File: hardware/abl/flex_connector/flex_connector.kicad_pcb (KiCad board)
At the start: 2 copper layers, 68.3 x 119.1 mm, 3 parts, among them J1 Conn_01x20_Pin, J2 Conn_01x20_Pin

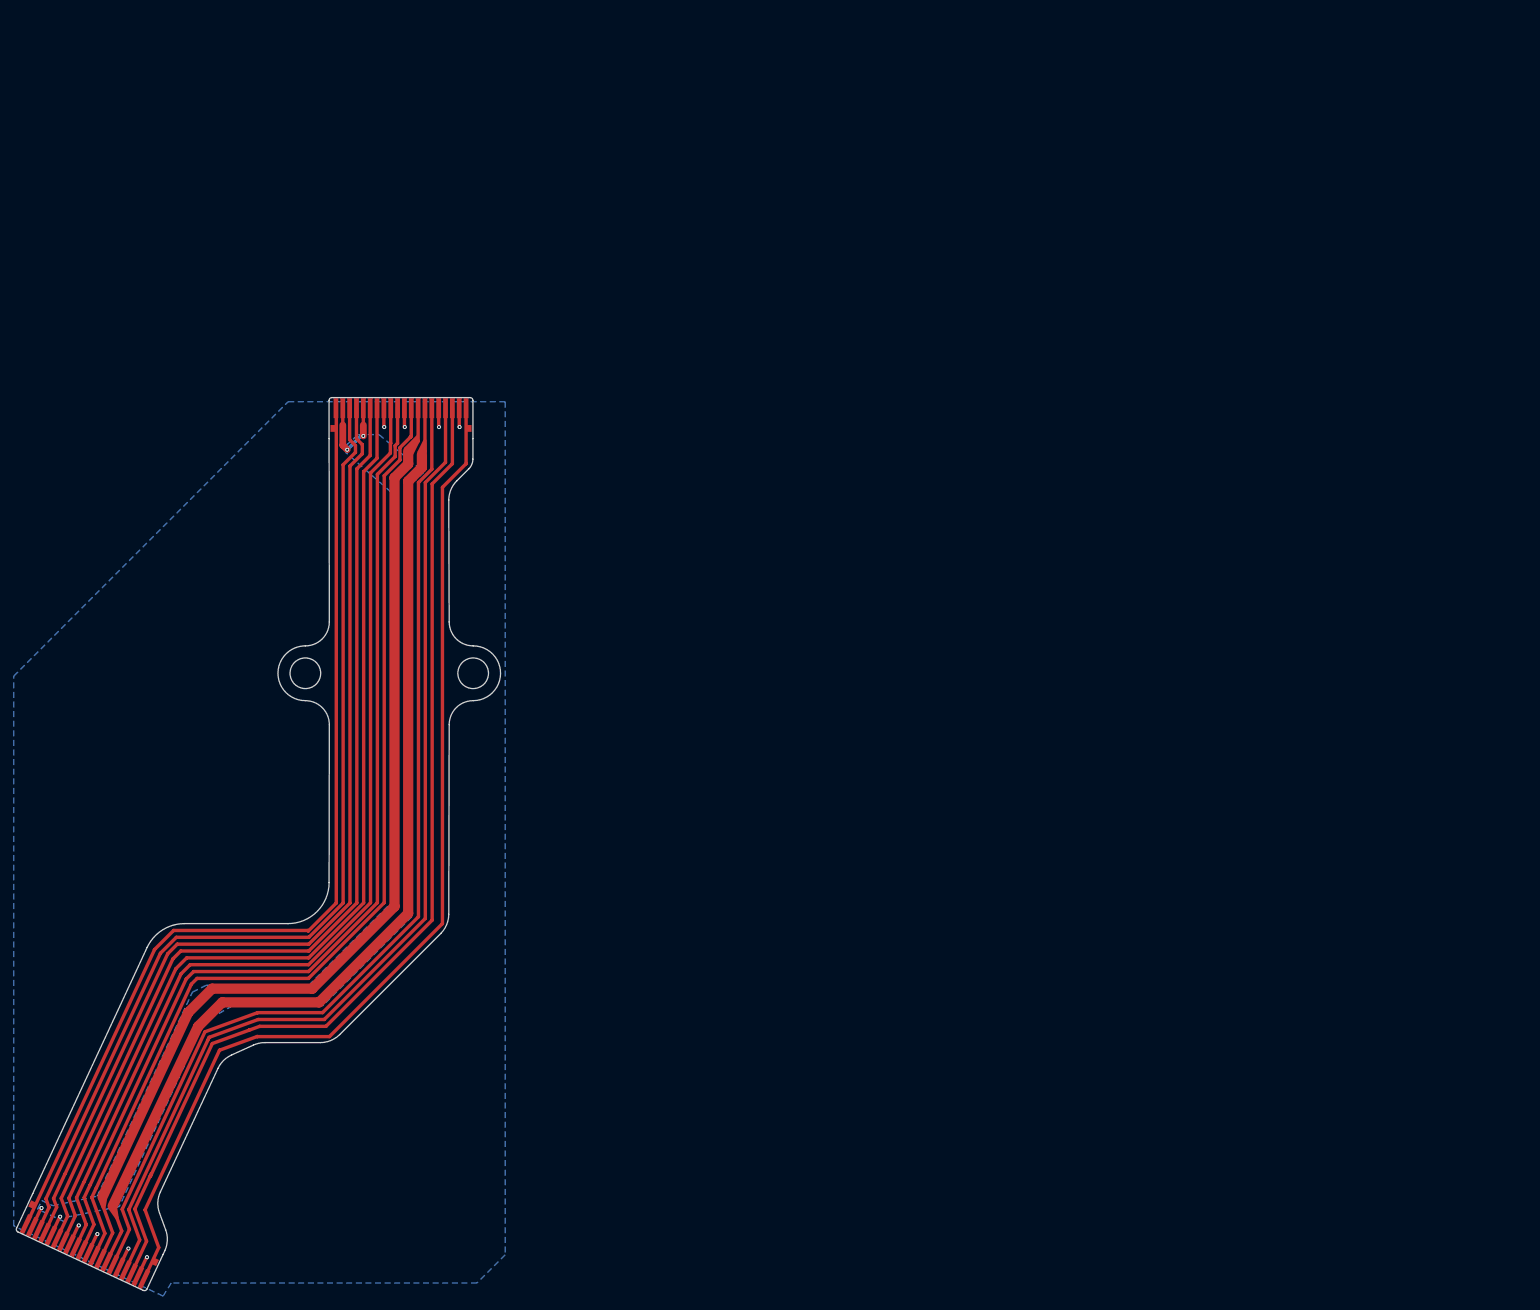
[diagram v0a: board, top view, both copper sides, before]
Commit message: Rename files, names and labels to be more consistent. Add READMEs for connectors and extend some other READMEs.
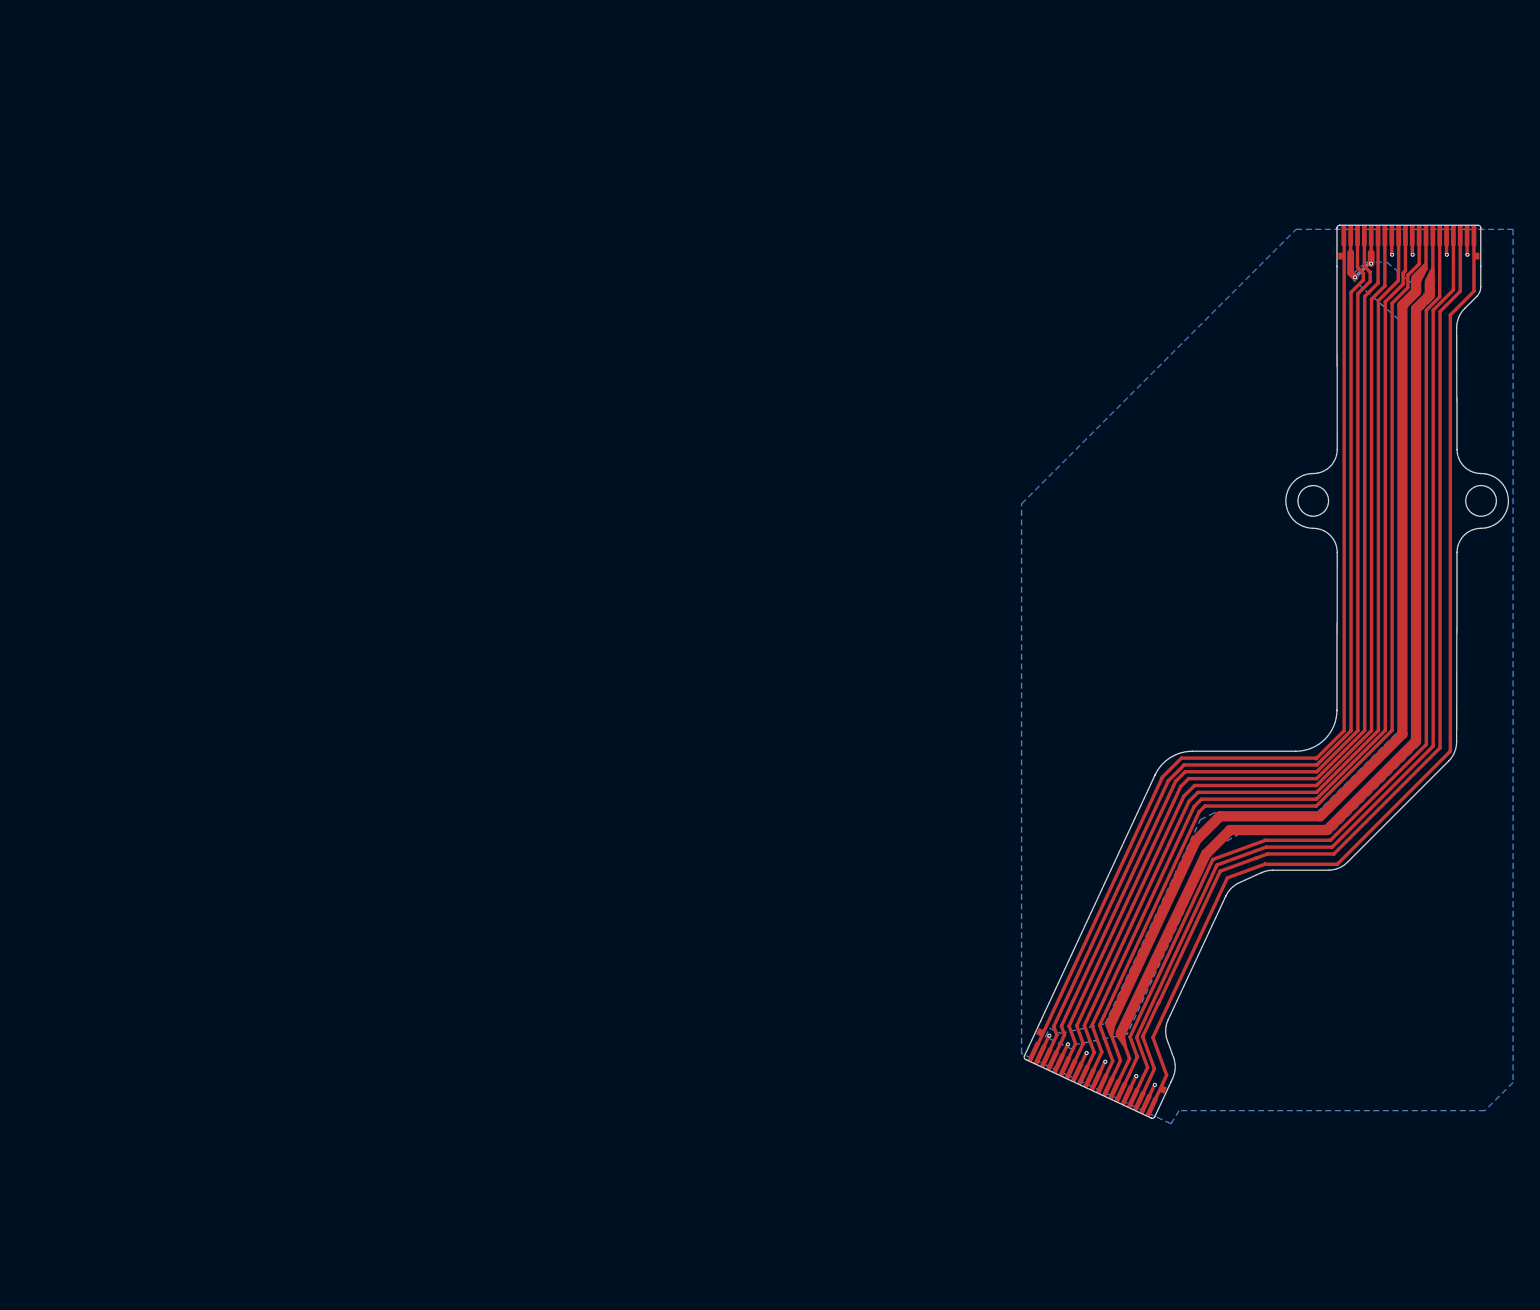
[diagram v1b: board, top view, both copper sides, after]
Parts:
- moved G*** 149.3 mm to (214.5, 93.2)
- moved J1 149.3 mm to (181.7, 163.0)
- moved J2 149.3 mm to (209.1, 38.6)
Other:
- board text added: "ABL Flex Connector v1.0"
- board text removed: "Flex Connector A v1.0"

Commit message: Add current renderings to all ABL PCBs.
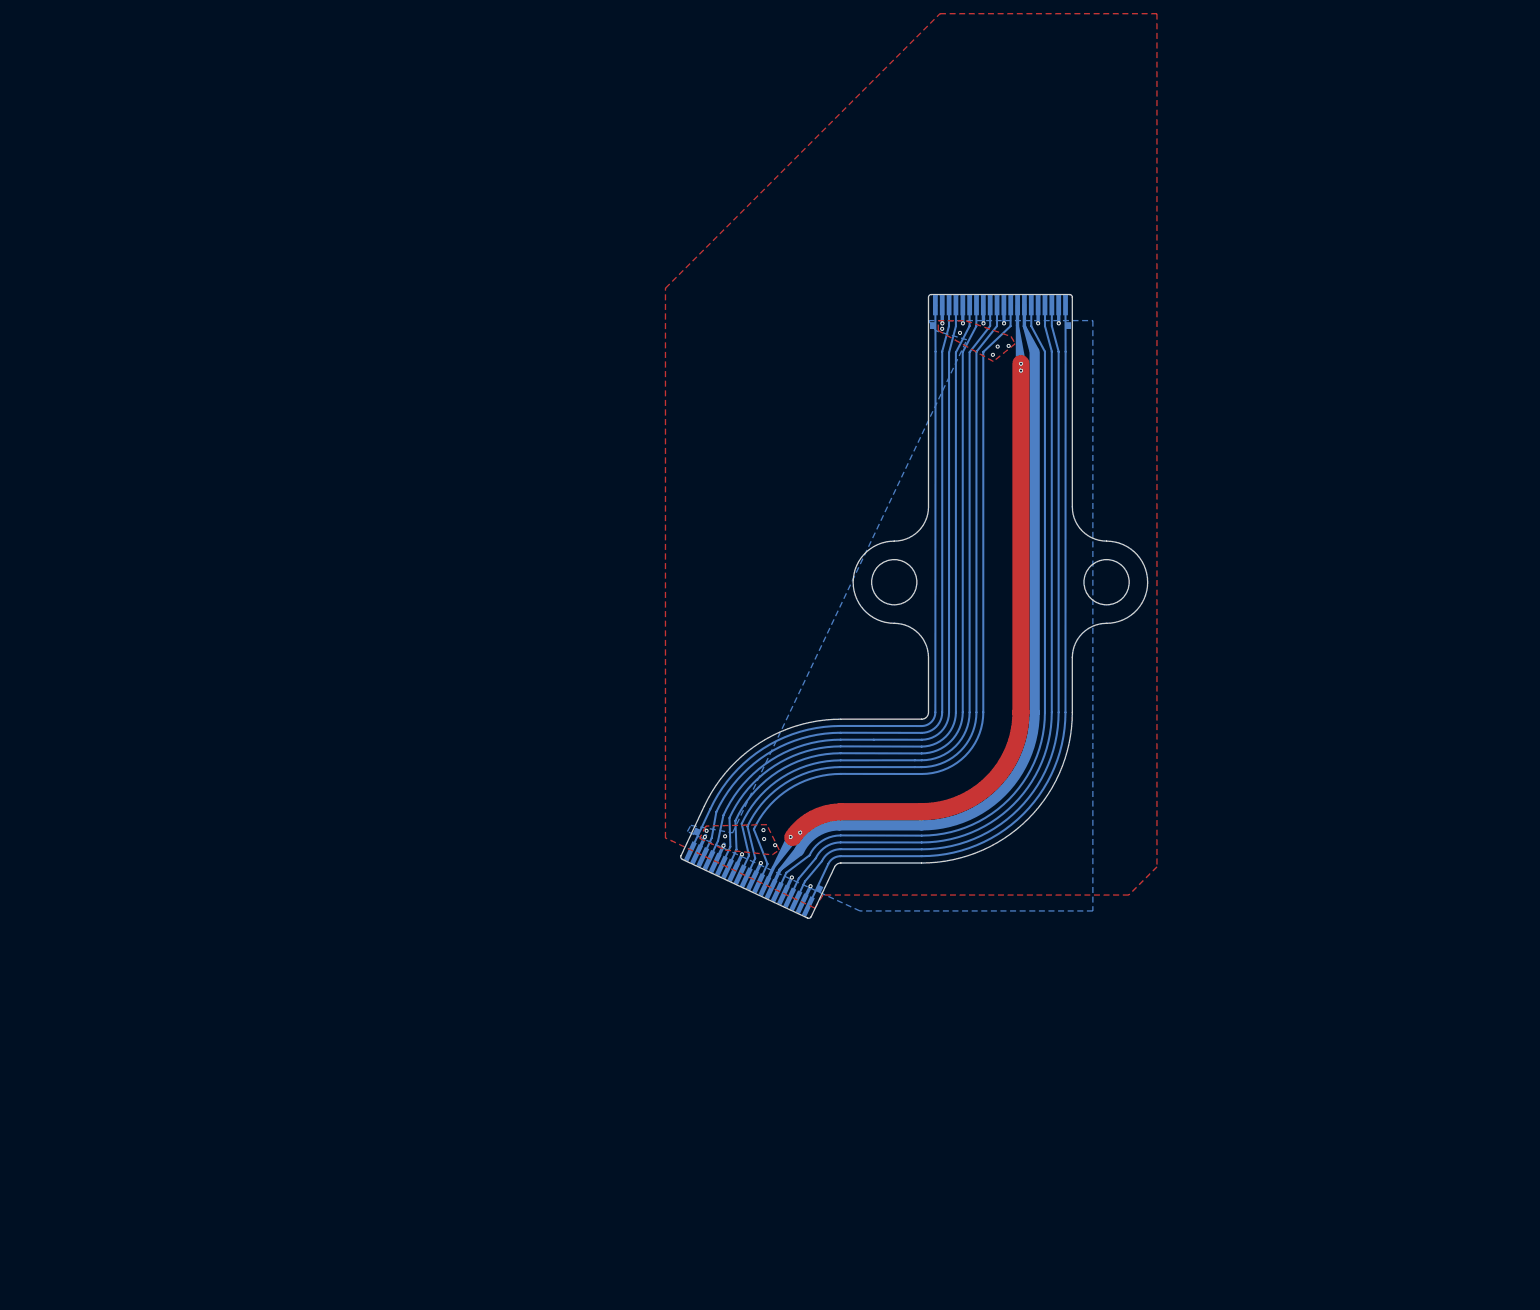
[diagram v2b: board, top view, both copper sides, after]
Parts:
- J1, J2: moved to B.Cu
- moved J1 67.4 mm to (121.7, 132.4), turned to -25 degrees
- moved G*** 53.6 mm to (161.6, 84.7)
- moved J2 50.6 mm to (159.0, 45.7), turned to 180 degrees
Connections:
- J1 pad 15: /i1 -> /i4
- J1 pad 17: /i2 -> /i3
- J1 pad 18: /i3 -> /i2
- J1 pad 20: /i4 -> /i1
- J2 pad 1: /i4 -> /i1
- J2 pad 3: /i3 -> /i2
- J2 pad 4: /i2 -> /i3
- J2 pad 6: /i1 -> /i4
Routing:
- net +5V: track 149.9 -> 71.6 mm, vias 0 -> 4
- net /SDA: track 152.8 -> 78.2 mm
- net /SCL: track 152.0 -> 78.5 mm
- net /ALERT: track 150.9 -> 78.5 mm
- net +3.3V: track 150.3 -> 78.6 mm
- net /ENABLE: track 149.7 -> 79.2 mm
- net /i1: track 148.0 -> 78.3 mm
- net /i2: track 147.7 -> 78.4 mm
- net /i3: track 147.4 -> 78.4 mm
- net /i7: track 149.2 -> 80.3 mm
- net /i5: track 148.0 -> 79.1 mm
- net /i6: track 149.0 -> 80.2 mm
- net /i8: track 150.2 -> 81.6 mm
- net /i4: track 145.7 -> 79.1 mm
- net +4V: track 19.3 -> 10.5 mm, vias 4 -> 14
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- added copper zone on F.Cu, net +4V
- added copper zone on F.Cu, net GND
- removed copper zone on B.Cu, net GND
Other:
- board size 68.3 x 119.1 mm -> 68.2 x 91.1 mm
- board text added: "+3.3V"
- board text added: "+5V"
- board text added: "Alert"
- board text added: "Enable"
- board text added: "GND"
- board text added: "SCL"
- board text added: "SDA"
- board text added: "VLED"
- board text added: "i1"
- board text added: "i2"
- board text added: "i3"
- board text added: "i4"
- board text added: "i5"
- board text added: "i6"
- board text added: "i7"
- board text added: "other side"

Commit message: Many small adjustments for the next production run.
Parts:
- moved G*** 124.8 mm to (39.1, 60.8), turned to -90 degrees
- moved J1 98.8 mm to (31.8, 91.3)
- moved J2 95.6 mm to (68.8, 14.3)
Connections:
- J1 pad 8: +5V -> +4V
- J2 pad 13: +5V -> +4V
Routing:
- net /i8: track 81.6 -> 9.87 mm
- net +5V: track 71.6 -> 0.00 mm, vias 4 -> 0
- net /i7: track 80.3 -> 9.87 mm
- net /i6: track 80.2 -> 9.87 mm
- net /ENABLE: track 79.2 -> 9.87 mm
- net /i5: track 79.1 -> 9.87 mm
- net /i4: track 79.1 -> 9.87 mm
- net +3.3V: track 78.6 -> 9.87 mm
- net /ALERT: track 78.5 -> 9.87 mm
- net /SCL: track 78.5 -> 9.87 mm
- net /i2: track 78.4 -> 9.87 mm
- net /i3: track 78.4 -> 9.87 mm
- net /i1: track 78.3 -> 9.94 mm
- net /SDA: track 78.2 -> 9.87 mm
- net GND: track 22.0 -> 50.8 mm, vias 8 -> 43
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- added copper zone on B.Cu, net GND
- removed copper zone on F.Cu, net +4V
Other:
- board size 68.2 x 91.1 mm -> 57.1 x 81.4 mm
- board text added: "ABL Flex Connector v1.1"
- board text added: "Into LED module"
- board text added: "Into controller module"
- board text added: "Pin numbering of this schematics / symbols contradicts that of the rigid PCBs, but the result should be all right."
- board text added: "https://beste-lampe.de"
- board text removed: "ABL Flex Connector v1.0"
- board text removed: "VLED"
- board text removed: "https://lenaschimmel.de/besteLampe!"
- board text removed: "other side"

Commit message: WIP feature conf (does not compile)
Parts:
- added REF**: TestPoint_Plated_Hole_D0.8mm, TestPoint:TestPoint_Plated_Hole_D0.8mm, F.Cu at (229.6, 62.9)
- added REF**: TestPoint_Plated_Hole_D0.8mm, TestPoint:TestPoint_Plated_Hole_D0.8mm, F.Cu at (217.4, 63.0)
- added REF**: TestPoint_Plated_Hole_D0.8mm, TestPoint:TestPoint_Plated_Hole_D0.8mm, F.Cu at (227.0, 67.3)
- added REF**: TestPoint_Plated_Hole_D0.8mm, TestPoint:TestPoint_Plated_Hole_D0.8mm, F.Cu at (213.9, 63.0)
- added REF**: TestPoint_Plated_Hole_D0.8mm, TestPoint:TestPoint_Plated_Hole_D0.8mm, F.Cu at (219.1, 61.4)
- added REF**: TestPoint_Plated_Hole_D0.8mm, TestPoint:TestPoint_Plated_Hole_D0.8mm, F.Cu at (226.1, 61.4)
- added REF**: TestPoint_Plated_Hole_D0.8mm, TestPoint:TestPoint_Plated_Hole_D0.8mm, F.Cu at (222.7, 78.9)
- added REF**: TestPoint_Plated_Hole_D0.8mm, TestPoint:TestPoint_Plated_Hole_D0.8mm, F.Cu at (212.1, 61.4)
- added REF**: TestPoint_Plated_Hole_D0.8mm, TestPoint:TestPoint_Plated_Hole_D0.8mm, F.Cu at (220.9, 63.0)
- added REF**: TestPoint_Plated_Hole_D0.8mm, TestPoint:TestPoint_Plated_Hole_D0.8mm, F.Cu at (224.4, 63.0)
- added REF**: TestPoint_Plated_Hole_D0.8mm, TestPoint:TestPoint_Plated_Hole_D0.8mm, F.Cu at (222.6, 61.4)
- added REF**: TestPoint_Plated_Hole_D0.8mm, TestPoint:TestPoint_Plated_Hole_D0.8mm, F.Cu at (227.9, 63.8)
- added REF**: TestPoint_Plated_Hole_D0.8mm, TestPoint:TestPoint_Plated_Hole_D0.8mm, F.Cu at (231.3, 61.4)
- added REF**: TestPoint_Plated_Hole_D0.8mm, TestPoint:TestPoint_Plated_Hole_D0.8mm, F.Cu at (215.6, 61.4)
- moved G*** 167.2 mm to (205.0, 81.8), turned to -160 degrees
- moved J1 161.0 mm to (186.8, 135.0)
- moved J2 156.8 mm to (221.8, 48.4)
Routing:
- net GND: track 50.8 -> 930.5 mm, vias 43 -> 92
- net /SDA: track 9.87 -> 102.0 mm
- net /SCL: track 9.87 -> 101.8 mm
- net /ALERT: track 9.87 -> 101.0 mm
- net /ENABLE: track 9.87 -> 100.9 mm
- net +3.3V: track 9.87 -> 100.6 mm
- net /i8: track 9.87 -> 100.0 mm
- net /i7: track 9.87 -> 99.5 mm
- net /i6: track 9.87 -> 98.0 mm
- net /i5: track 9.87 -> 97.4 mm
- net /i4: track 9.87 -> 96.0 mm
- net /i3: track 9.87 -> 94.0 mm
- net /i1: track 9.94 -> 94.0 mm
- net /i2: track 9.87 -> 93.2 mm
- net +4V: track 6.95 -> 15.1 mm, vias 13 -> 6
- added copper zone on F.Cu, net +4V
- removed copper zone on B.Cu, net +4V
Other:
- board size 57.1 x 81.4 mm -> 55 x 91 mm
- board text added: "(there is no test pad for +5V)"
- board text added: "3.3V"
- board text added: "ABL Flex Connector"
- board text added: "Al"
- board text added: "En"
- board text added: "i8"
- board text added: "v1.2"
- board text removed: "+3.3V"
- board text removed: "ABL Flex Connector v1.1"
- board text removed: "Enable"
